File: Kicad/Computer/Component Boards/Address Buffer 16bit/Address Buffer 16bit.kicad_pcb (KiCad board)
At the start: 2 copper layers, 18.8 x 53.5 mm, 20 parts, among them CN1 CA0612KRX7R9BB100, CN2 CA0612KRX7R9BB100, CN3 CA0612KRX7R9BB100, CN4 CA0612KRX7R9BB100, IC1 SN74ABT245BDBR, IC2 SN74ABT245BDBR, IC5 AP7365-33WG-7, J1 Conn_02x20_Counter_Clockwise

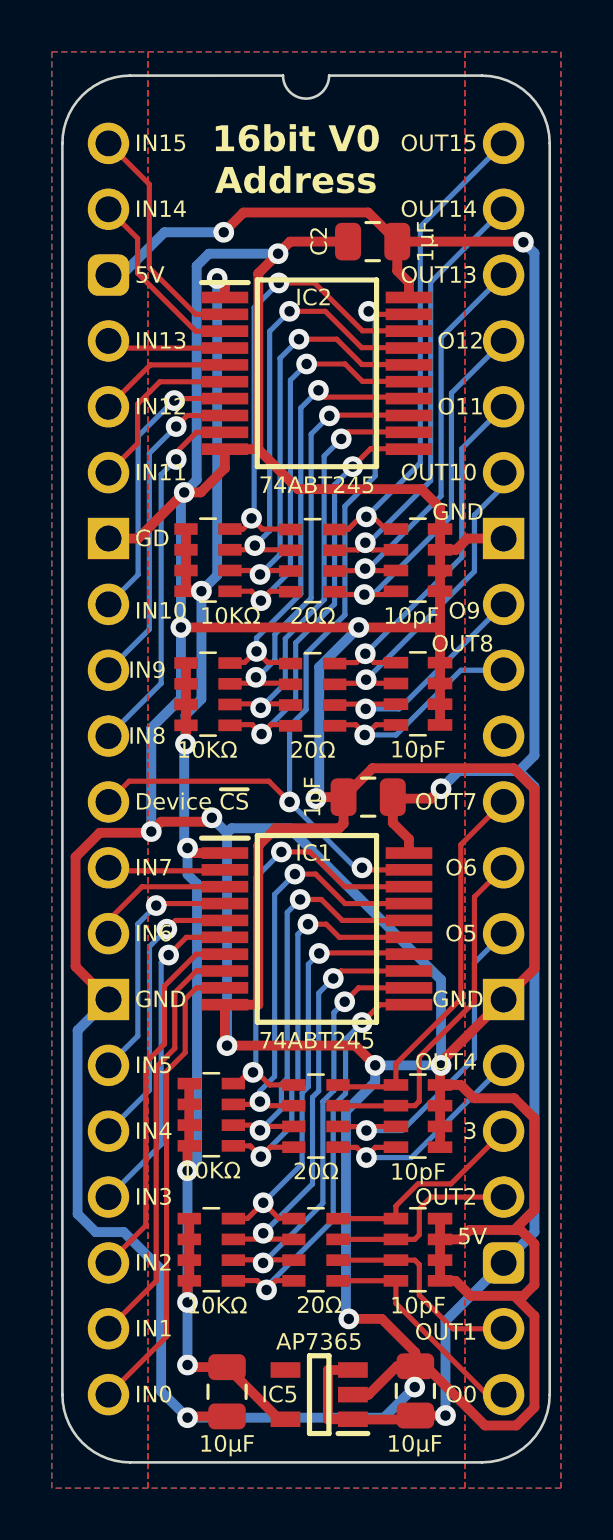
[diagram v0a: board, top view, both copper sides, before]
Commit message: Removed some component copper fills.
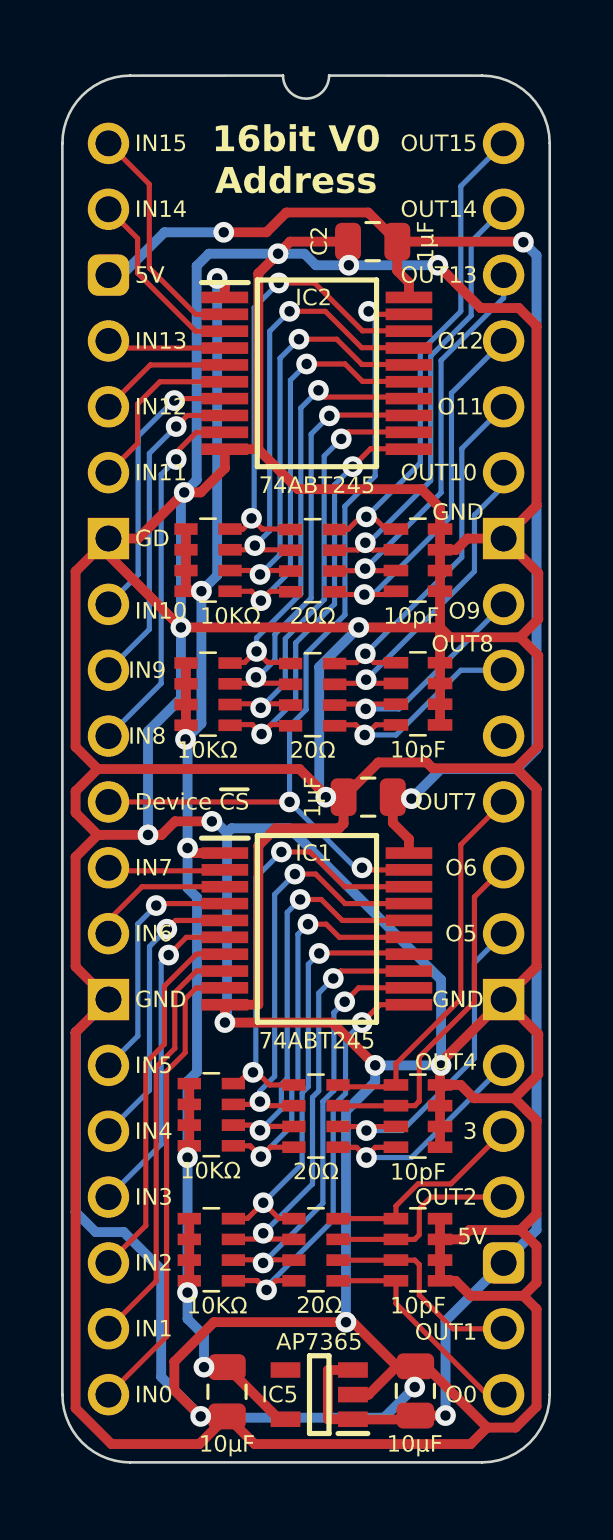
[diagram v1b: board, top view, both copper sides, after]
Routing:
- net GND: track 240.6 -> 347.1 mm, vias 13 -> 15
- net /3.3V: track 62.3 -> 60.9 mm
- net Device ~{CS}: track 35.3 -> 34.7 mm
- removed copper zone on B.Cu, net GND
- removed copper zone on F.Cu, net GND

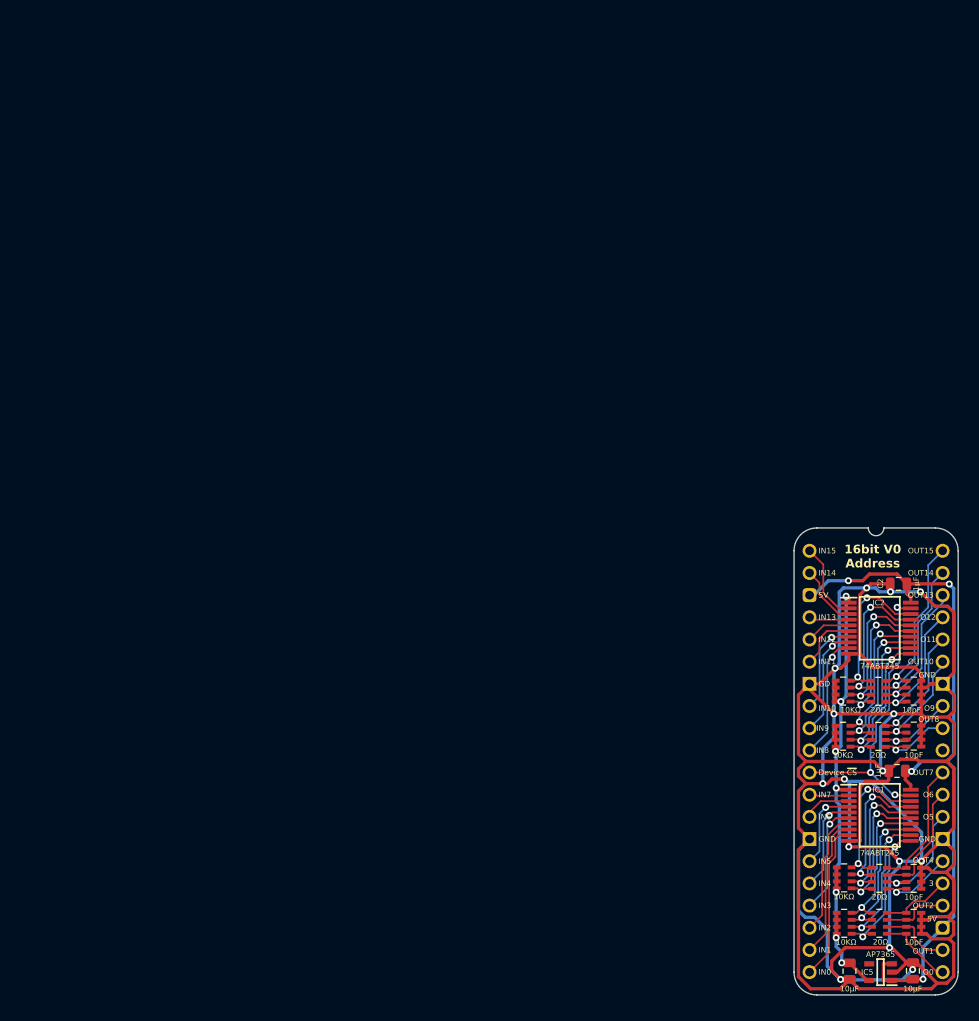
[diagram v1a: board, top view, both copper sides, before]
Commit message: Use VRML instead of STEPs for Processor Board models.
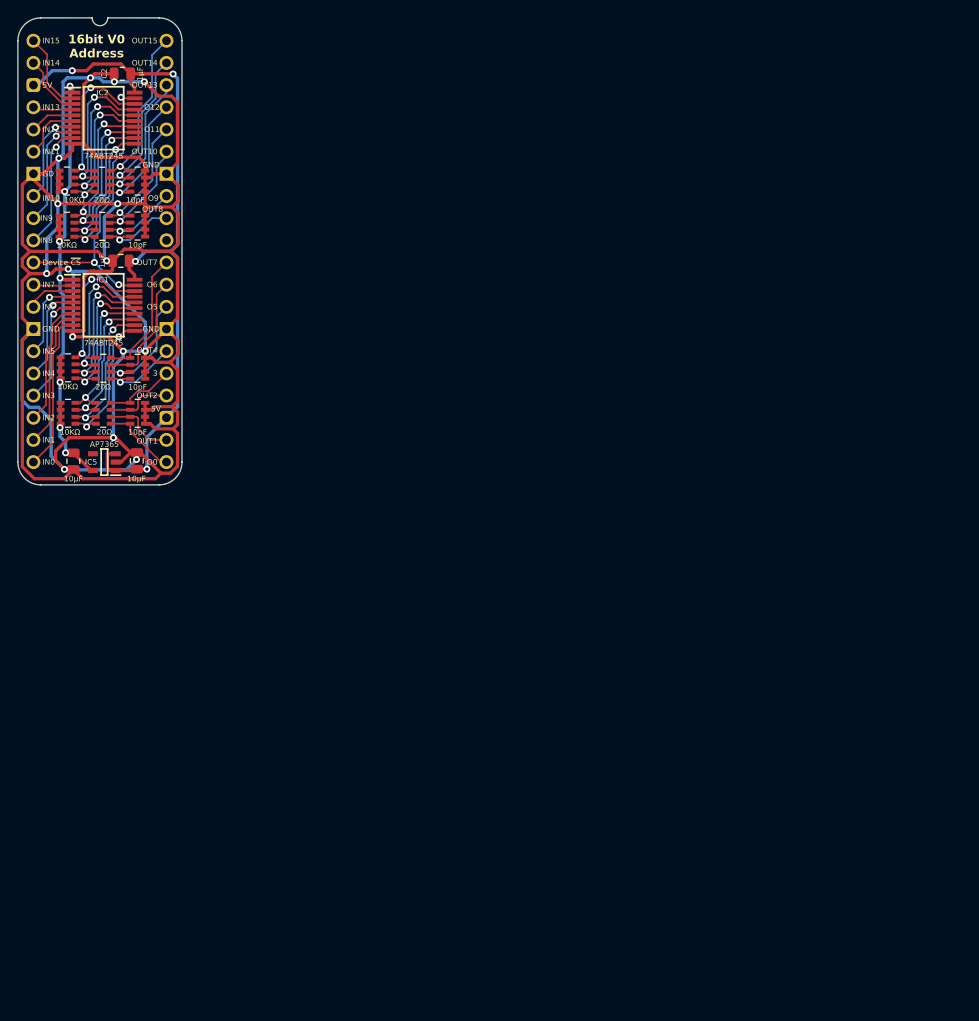
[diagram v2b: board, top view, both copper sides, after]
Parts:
- added J2: Pin_Header_01x20, SamacSys_Parts:PinHeader_1x20_P2.54mm_Vertical, B.Cu at (15.2, 0.00)
- added J3: Pin_Header_01x20, SamacSys_Parts:PinHeader_1x20_P2.54mm_Vertical, B.Cu at (0.00, 0.00)
- moved C1 106.4 mm to (10.0, 25.2)
- moved C8 106.4 mm to (11.8, 48.1)
- moved IC1 106.4 mm to (8.04, 30.3)
- moved IC2 106.4 mm to (8.04, 8.87)
- moved IC5 106.4 mm to (8.13, 48.3)
- moved J1 106.4 mm to (0.00, 0.00)
- moved RN1 106.4 mm to (3.94, 37.5)
- moved RN10 106.4 mm to (7.87, 16.1)
- moved RN2 106.4 mm to (3.94, 42.7)
- moved RN9 106.4 mm to (7.87, 21.2)
- moved C2 106.4 mm to (10.2, 3.79)
- moved C9 106.4 mm to (4.57, 48.1)
- moved CN1 106.4 mm to (11.9, 37.5)
- moved CN2 106.4 mm to (11.9, 42.7)
- moved CN3 106.4 mm to (11.9, 21.2)
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
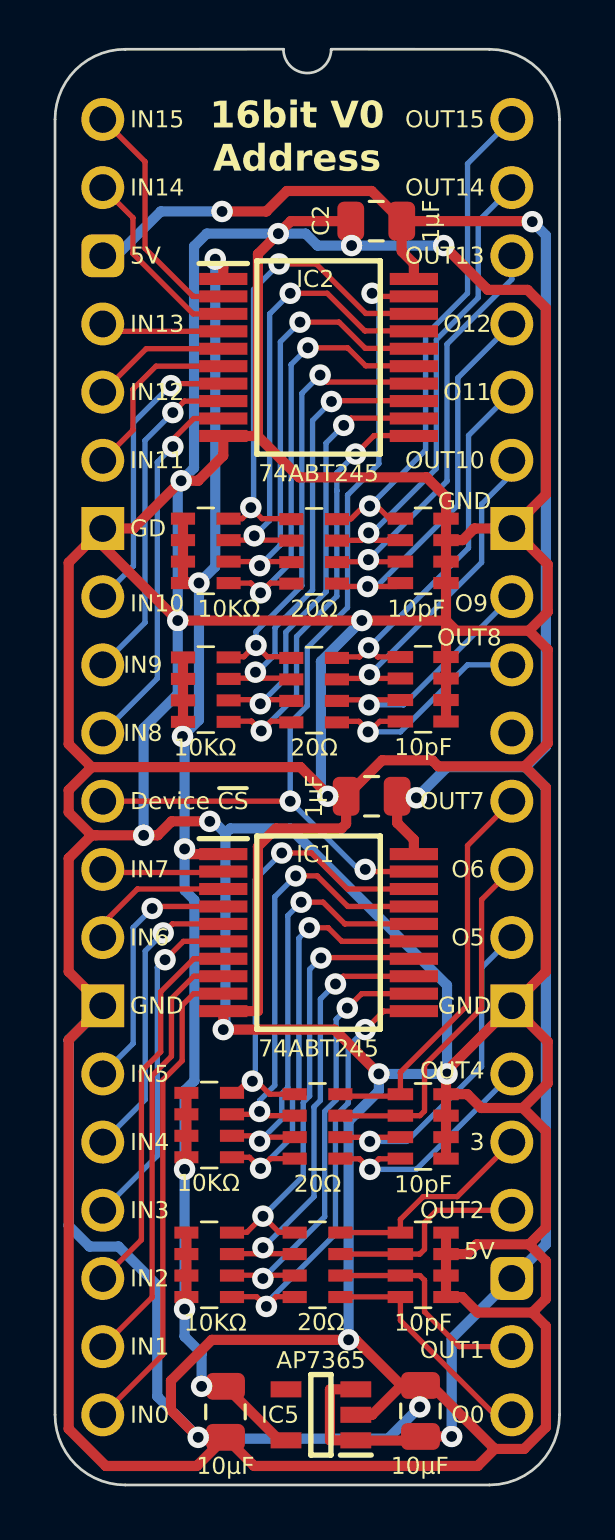
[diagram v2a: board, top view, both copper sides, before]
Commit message: Rounded 16 bit address buffer traces.
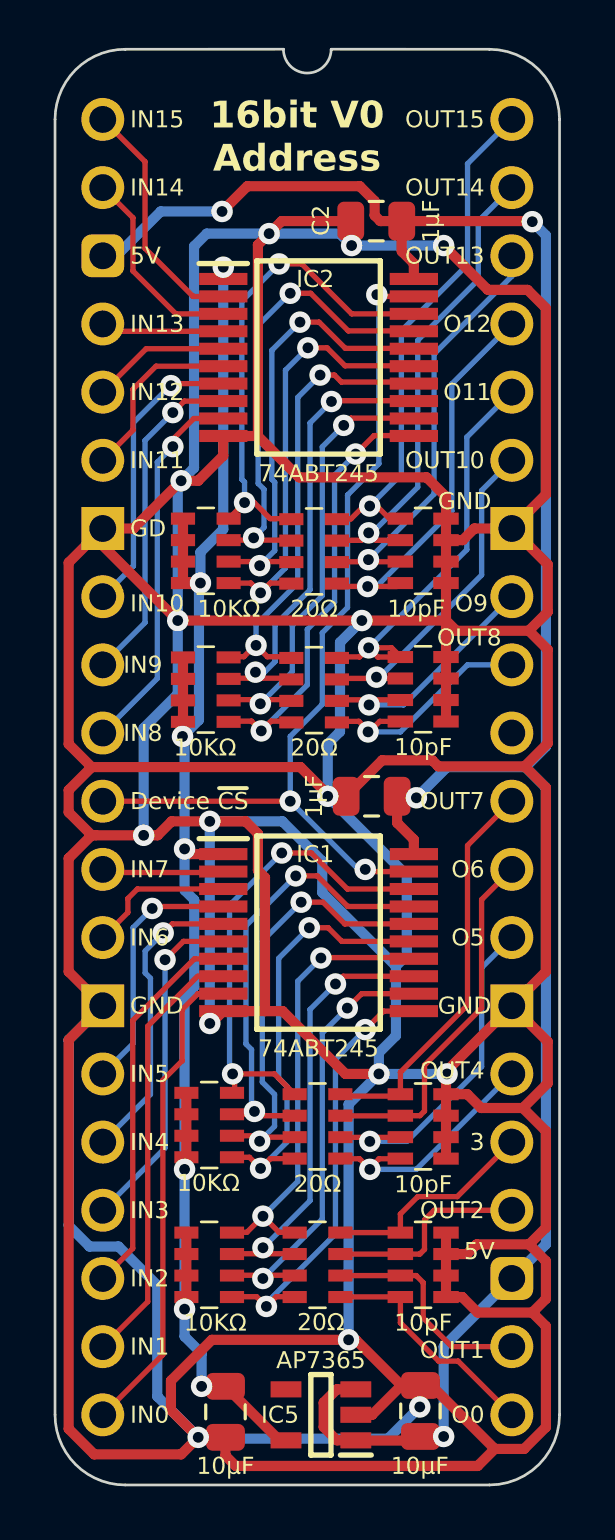
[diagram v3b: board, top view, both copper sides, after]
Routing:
- net GND: track 347.1 -> 350.4 mm
- net A11_{s}: track 14.4 -> 15.7 mm
- net /A7: track 17.1 -> 18.0 mm
- net A0_{s}: track 8.18 -> 8.87 mm
- net /3.3V: track 60.9 -> 60.4 mm
- net A6_{IN}: track 5.03 -> 5.54 mm

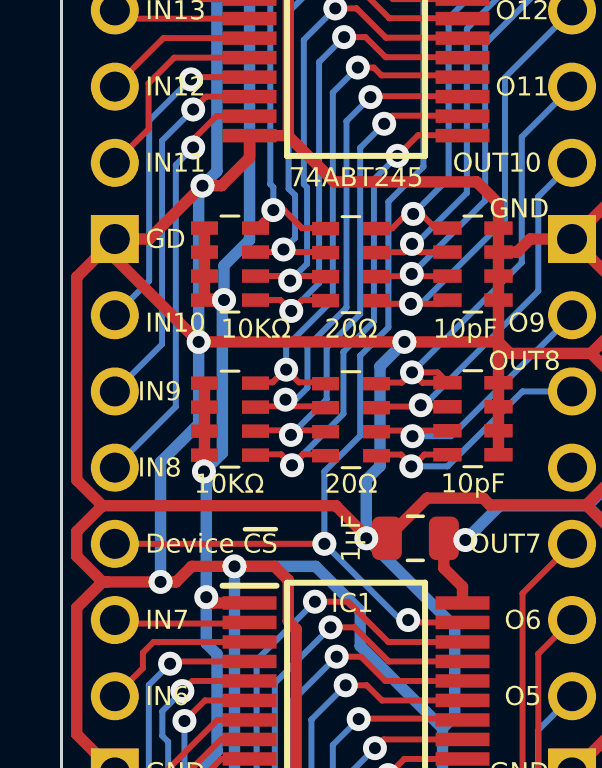
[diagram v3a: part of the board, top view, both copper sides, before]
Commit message: Converted a whole lot of boards to Kicad 9.0
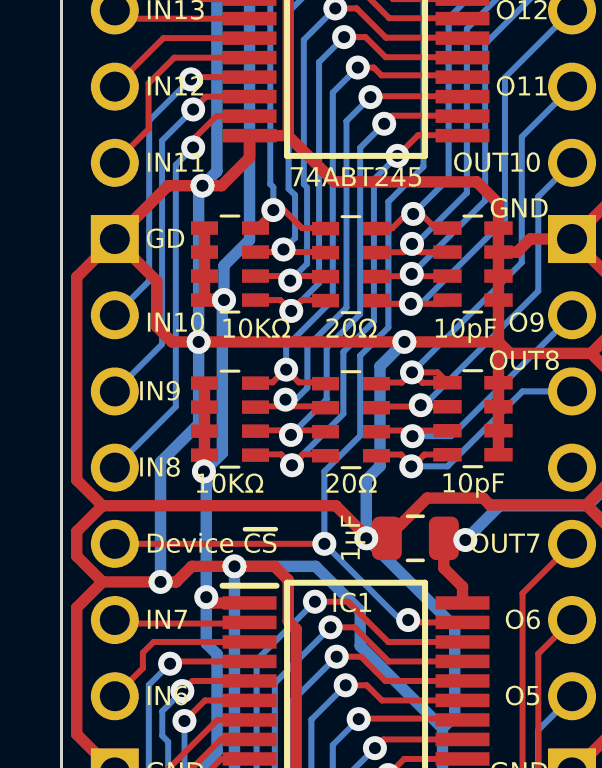
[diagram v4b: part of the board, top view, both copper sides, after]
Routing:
- net GND: track 350.4 -> 351.0 mm

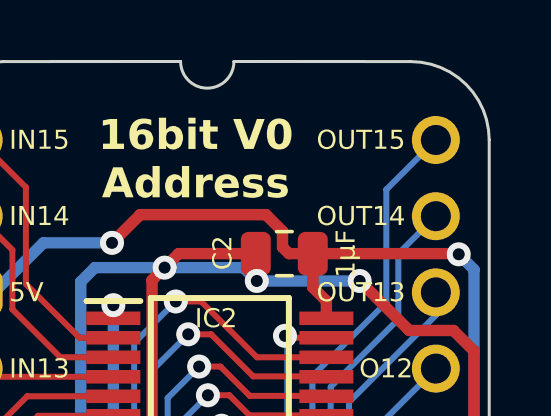
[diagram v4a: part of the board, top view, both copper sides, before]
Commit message: Changing component board sockets.
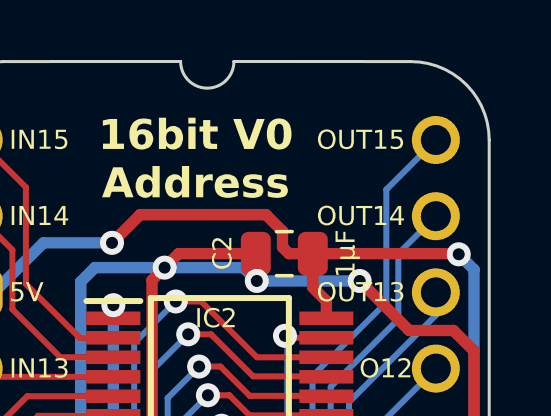
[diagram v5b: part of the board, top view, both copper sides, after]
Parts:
- removed J2, J3: Pin_Header_01x20, SamacSys_Parts:PinHeader_1x20_P2.54mm_Vertical
- J1: value Conn_02x20_Counter_Clockwise -> Board 2x20 W15.24mm

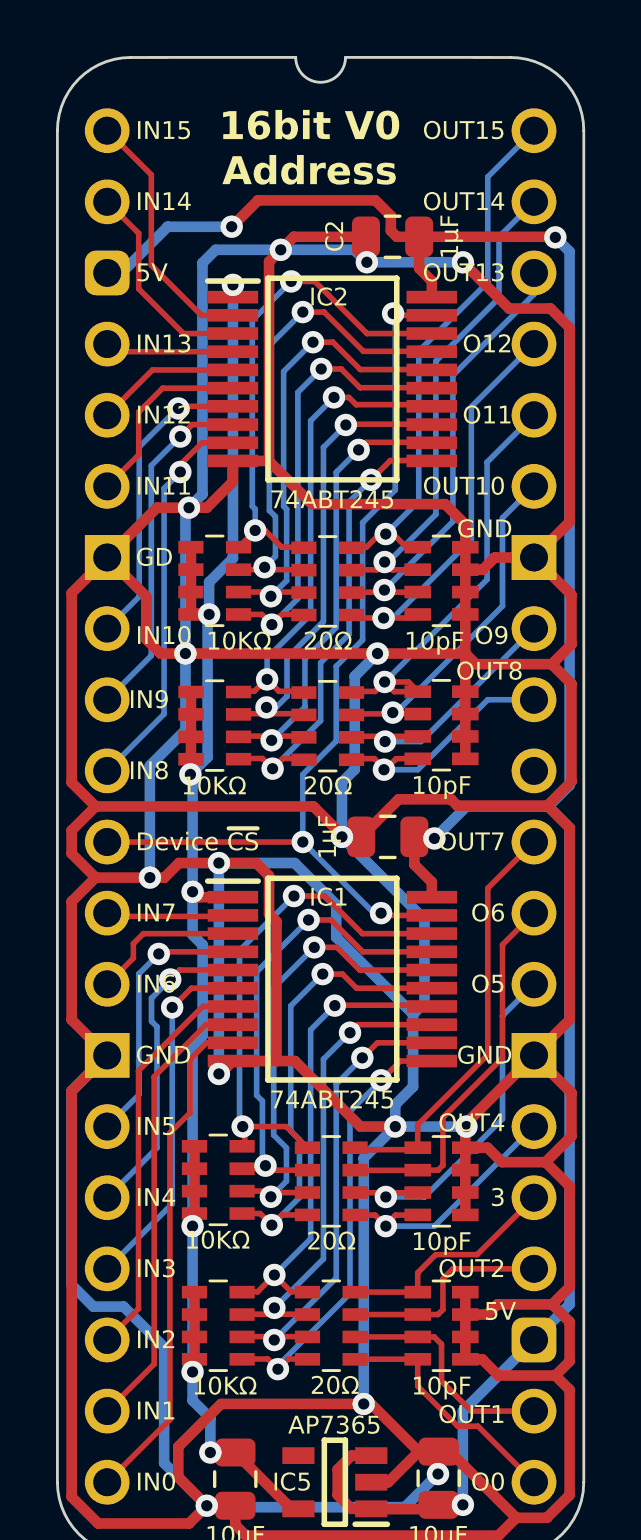
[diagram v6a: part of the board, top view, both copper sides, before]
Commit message: Added a board presence reader to the Processor Board.
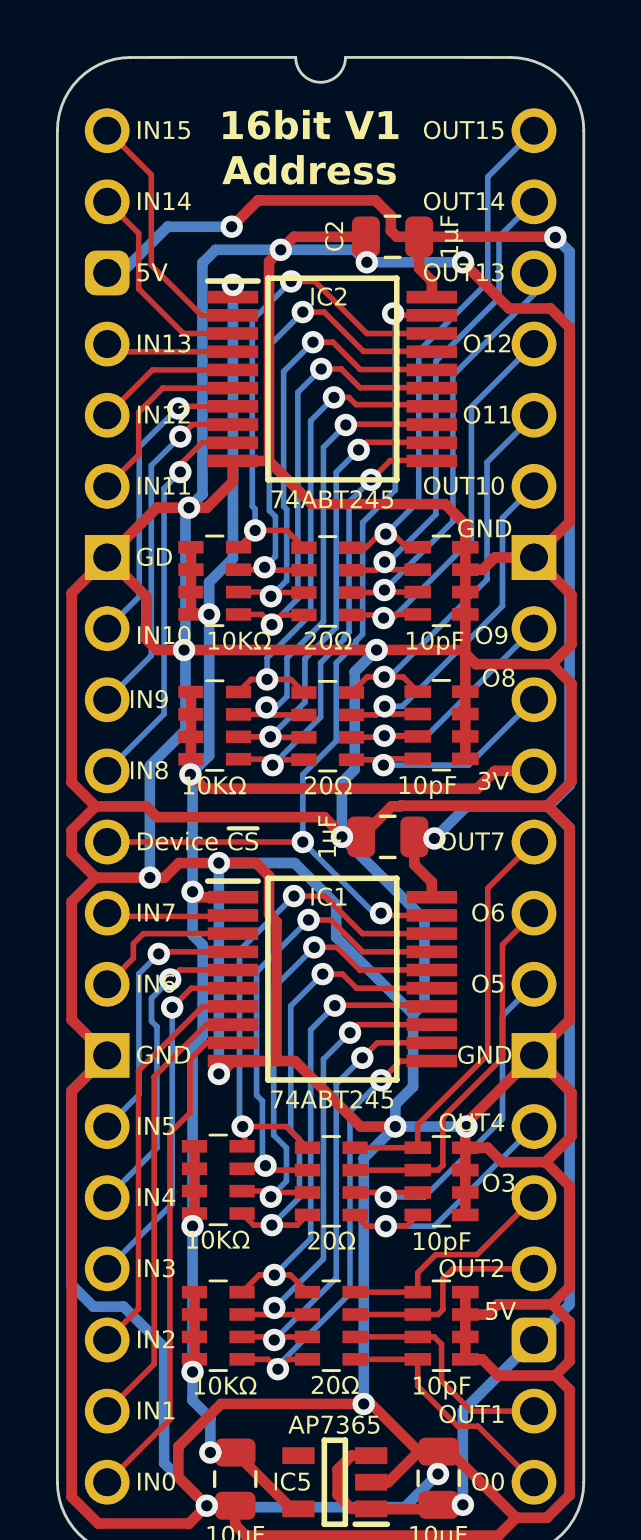
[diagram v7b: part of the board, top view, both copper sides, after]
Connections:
- C9 pad 1: /3.3V -> 3.3V
- IC1 pad 1: /3.3V -> 3.3V
- IC2 pad 1: /3.3V -> 3.3V
- IC5 pad 5: /3.3V -> 3.3V
- J1 pad 31: unconnected-(J1-Pad31) -> 3.3V
- RN1 pad 5: /3.3V -> 3.3V
- RN1 pad 6: /3.3V -> 3.3V
- RN1 pad 7: /3.3V -> 3.3V
- RN1 pad 8: /3.3V -> 3.3V
- RN2 pad 5: /3.3V -> 3.3V
- RN2 pad 6: /3.3V -> 3.3V
- RN2 pad 7: /3.3V -> 3.3V
- RN2 pad 8: /3.3V -> 3.3V
- RN3 pad 5: /3.3V -> 3.3V
- RN3 pad 6: /3.3V -> 3.3V
- RN3 pad 7: /3.3V -> 3.3V
- RN3 pad 8: /3.3V -> 3.3V
- RN4 pad 5: /3.3V -> 3.3V
- RN4 pad 6: /3.3V -> 3.3V
- RN4 pad 7: /3.3V -> 3.3V
- RN4 pad 8: /3.3V -> 3.3V
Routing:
- net 3.3V: track 0.00 -> 73.1 mm, vias 0 -> 7
- net /3.3V: track 60.4 -> 0.00 mm, vias 7 -> 0
- net A11_{s}: track 15.7 -> 14.5 mm
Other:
- board text added: "16bit V1 Address"
- board text added: "3V"
- board text added: "O3"
- board text added: "O8"
- board text removed: "16bit V0 Address"
- board text removed: "3"
- board text removed: "OUT8"
